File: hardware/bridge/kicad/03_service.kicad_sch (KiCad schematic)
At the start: 7 parts, among them SW2 BOOT, SW3 PAIR

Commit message: fix: close hardware rail-fault paths and sensor contract gaps
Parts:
- removed R11: 22, CANView:Resistor_SMD__R_0402_1005Metric, symbol CANView:CANView_bridge_R11
- added R15: 2.2k, CANView:Resistor_SMD__R_0402_1005Metric, symbol CANView:CANView_bridge_R15
- R13: value 10k -> 22; MPN GEN-R-0402-10k-1% -> GEN-R-0402-22-1%
- R14: value 2.2k -> 10k; MPN GEN-R-0402-2.2k-1% -> GEN-R-0402-10k-1%
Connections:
- net 3V3: now also R14.1; no longer R13.1
- net LED_A: now also R15.2; no longer R14.2
- net PAIR_BUTTON_N: now also R14.2; no longer R13.2
- net STATUS_LED: now also R15.1; no longer R14.1
- net USB_DM: now also R12.2
- net USB_DM_CONN: now also R12.1
- net USB_DP: now also R13.2; no longer R12.2
- net USB_DP_CONN: now also R13.1; no longer R12.1
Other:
- moved on the sheet: R12, R13, R14

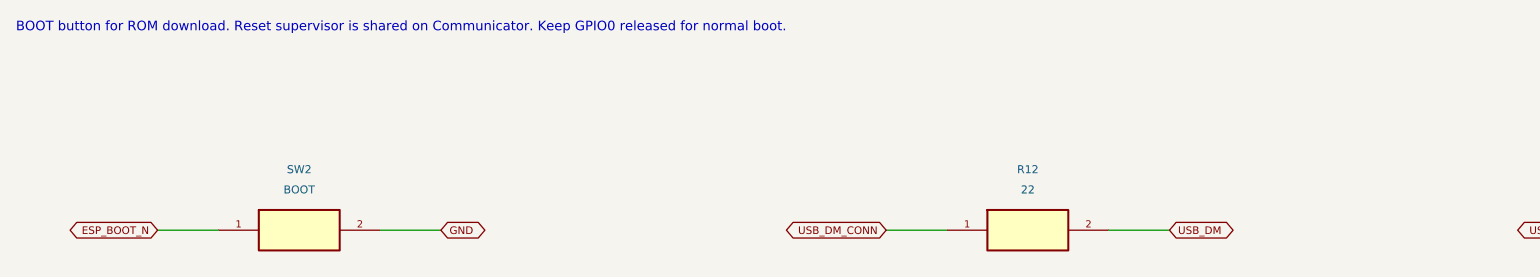
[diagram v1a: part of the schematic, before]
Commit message: Design independent OTA recovery and update N16R8 hardware
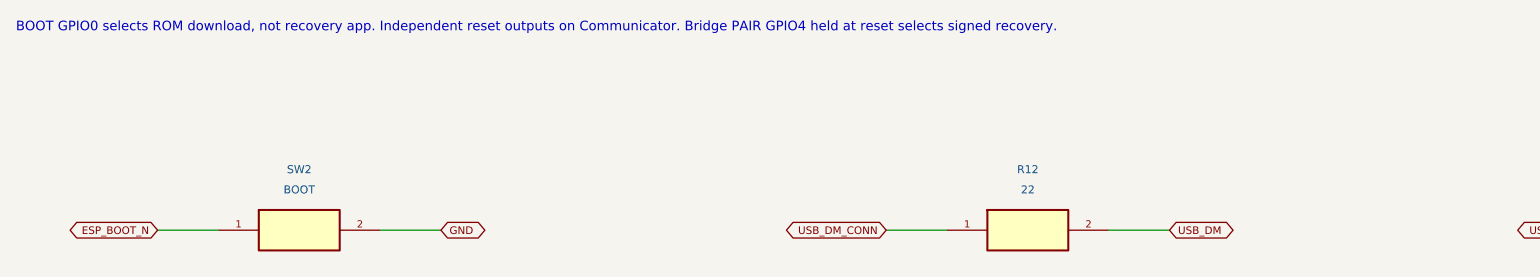
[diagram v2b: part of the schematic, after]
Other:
- note added: "BOOT GPIO0 selects ROM download, not recovery app. Independent reset outputs on Communicator. Bridge PAIR GPIO4 held at reset selects signed recovery."
- note removed: "BOOT button for ROM download. Reset supervisor is shared on Communicator. Keep GPIO0 released for normal boot."
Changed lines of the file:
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@@
 (kicad_sch (version 20250114) (generator "eeschema") (generator_version "10.0") (paper "A3") (title_block (title "CANView / 03_service") (date "2026-09-05") (rev "R1 REVIEW") (company "digitie/canview") (comment 1 "SCHEMATIC REVIEW ONLY - PCB/HIL release gates remain open"))
-(text "BOOT button for ROM download. Reset supervisor is shared on Communicator. Keep GPIO0 released for normal boot." (at 15.24 15.24 0) (effects (font (size 1.2 1.2)) (justify left)))
+(text "BOOT GPIO0 selects ROM download, not recovery app. Independent reset outputs on Communicator. Bridge PAIR GPIO4 held at reset selects signed recovery." (at 15.24 15.24 0) (effects (font (size 1.2 1.2)) (justify left)))
 (symbol (lib_id "CANView:CANView_bridge_SW2") (at 50.8000 40.6400 0) (unit 1) (in_bom yes) (on_board yes) (dnp no) (property "Reference" "SW2" (at 50.8000 33.0200 0)  (effects (font (size 1.0 1.0)) ))(property "Value" "BOOT" (at 50.8000 35.5600 0)  (effects (font (size 1.0 1.0)) ))(property "Footprint" "CANView:Button_Switch_SMD__SW_SPST_TL3342" (at 50.8000 40.6400 0) (hide yes) (effects (font (size 1.0 1.0)) ))(property "MPN" "TL3342F160QG" (at 50.8000 40.6400 0) (hide yes) (effects (font (size 1.0 1.0)) ))(property "Specification" "Momentary normally open; logic signal only" (at 50.8000 40.6400 0) (hide yes) (effects (font (size 1.0 1.0)) ))(property "Source" "" (at 50.8000 40.6400 0) (hide yes) (effects (font (size 1.0 1.0)) ))(property "Assembly" "FIT" (at 50.8000 40.6400 0) (hide yes) (effects (font (size 1.0 1.0)) ))(instances (project "bridge" (path "/695535dc-1835-5369-a035-dbad415d33c6/f45837cc-a8bb-5c7e-bc52-15102e8ffa7d" (reference "SW2") (unit 1)))))
 (wire (pts (xy 40.6400 40.6400) (xy 33.0200 40.6400)) (stroke (width 0) (type default)))
